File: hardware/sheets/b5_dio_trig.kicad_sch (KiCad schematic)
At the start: 26 parts, among them J7 Panel link 2x20 female, J8 Panel link 2x20 female, U501 SN74AHCT541PWR, U502 74HCT125PW, U503 SN74LVC1T45DBVR, U505 TCA9535PWR

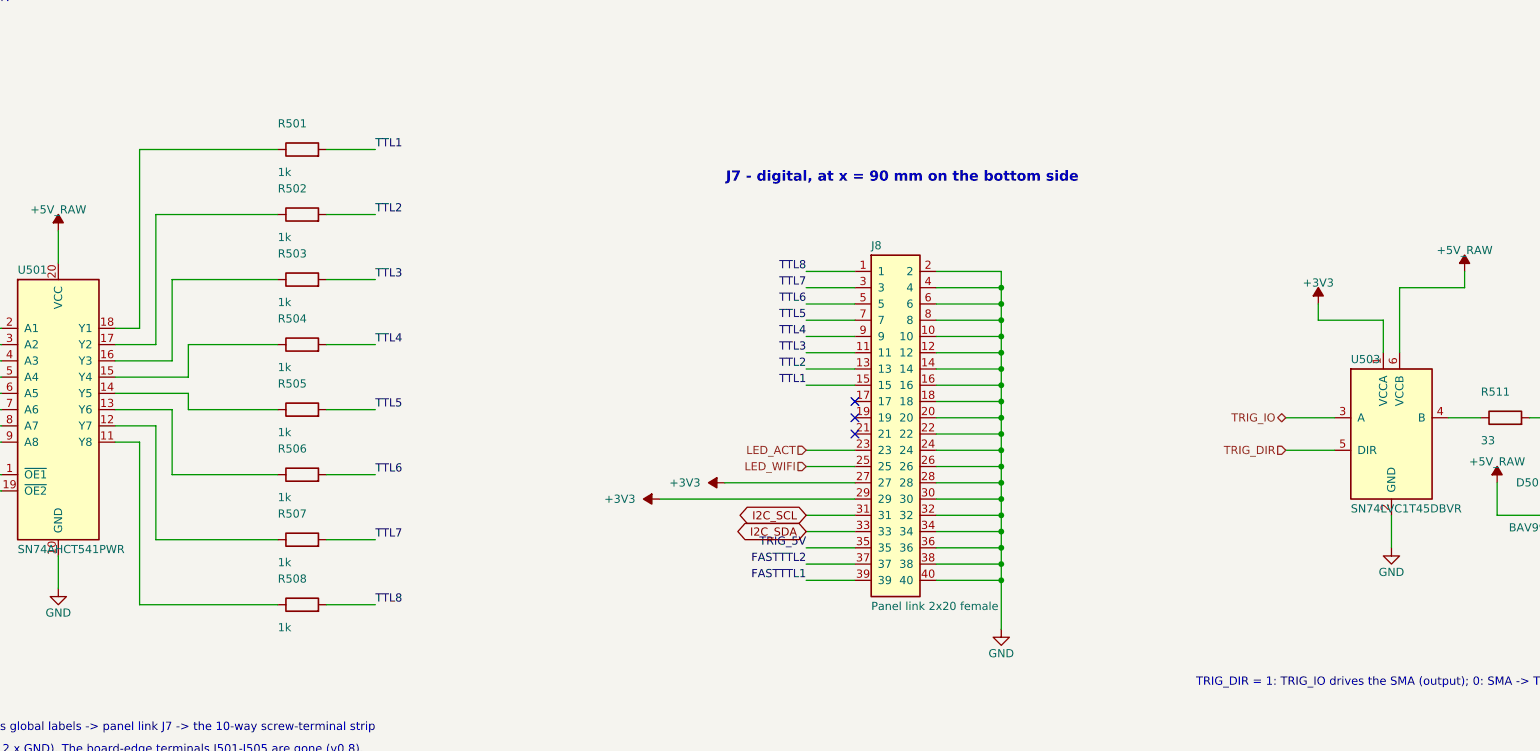
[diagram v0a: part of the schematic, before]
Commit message: b5: TTL series resistors R501-R508 as two 4 x 1k arrays RN501/RN502 (0603x4, C20197); U501 outputs labelled TTL1_Y..TTL8_Y (user request); same connectivity, ERC unchanged
Co-Authored-By: Claude Fable 5.1 <noreply@anthropic.com>
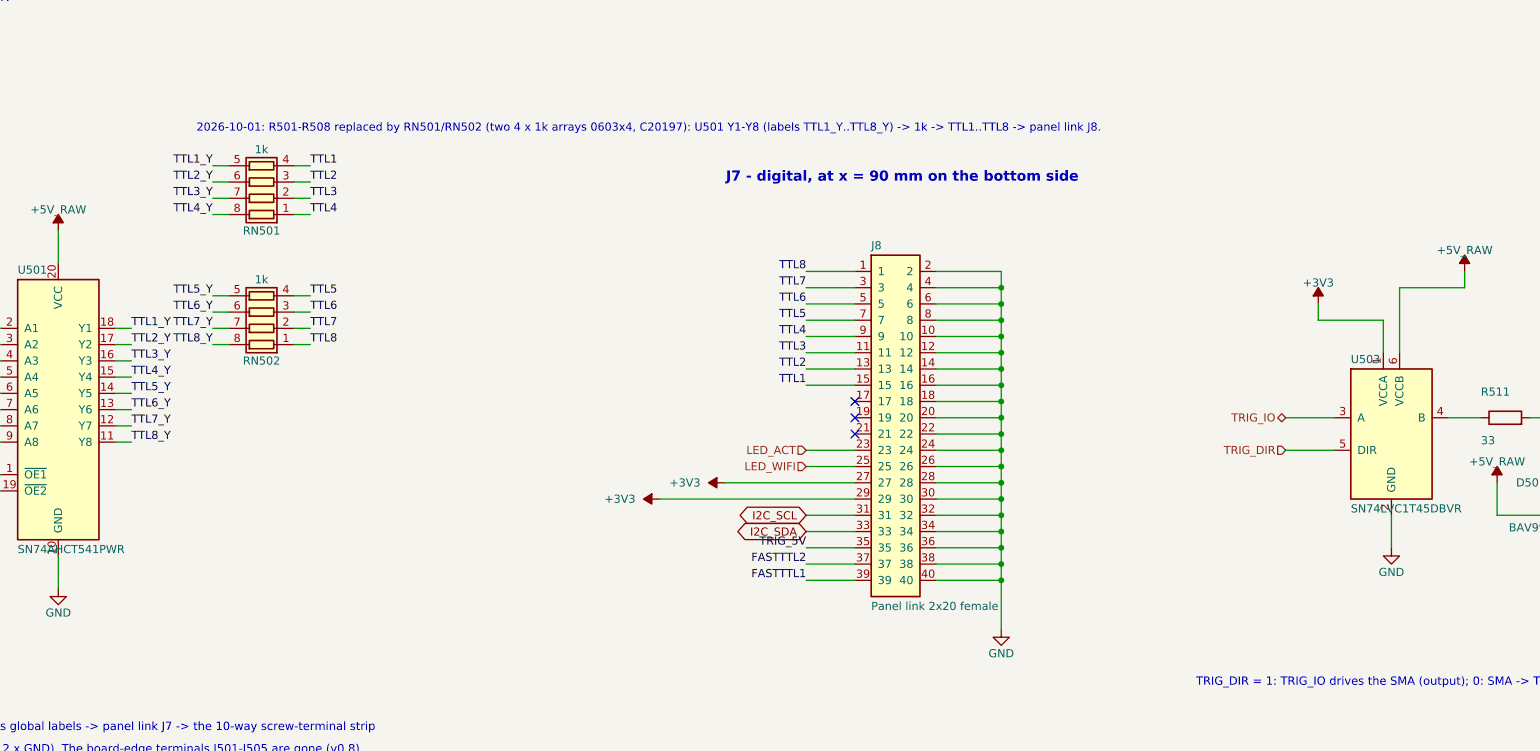
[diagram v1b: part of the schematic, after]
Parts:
- removed R501, R502, R503, R504, R505, R506, R507, R508: 1k, Resistor_SMD:R_0603_1608Metric, symbol class_board:R0603_1k
- added RN501, RN502: 1k, Resistor_SMD:R_Array_Convex_4x0603, symbol Device:R_Pack04
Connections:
- net TTL1: now also RN501.4 (R4.1)
- net TTL2: now also RN501.3 (R3.1)
- net TTL3: now also RN501.2 (R2.1)
- net TTL4: now also RN501.1 (R1.1)
- net TTL5: now also RN502.4 (R4.1)
- net TTL6: now also RN502.3 (R3.1)
- net TTL7: now also RN502.2 (R2.1)
- net TTL8: now also RN502.1 (R1.1)
- net TTL7_Y: now reaches U501.12 (Y7)
- net TTL7_Y: now also RN502.7 (R2.2)
- net TTL8_Y: now reaches U501.11 (Y8)
- net TTL8_Y: now also RN502.8 (R1.2)
- net TTL6_Y: now reaches U501.13 (Y6)
- net TTL6_Y: now also RN502.6 (R3.2)
- net TTL5_Y: now reaches U501.14 (Y5)
- net TTL5_Y: now also RN502.5 (R4.2)
- net TTL4_Y: now reaches U501.15 (Y4)
- net TTL4_Y: now also RN501.8 (R1.2)
- net TTL3_Y: now reaches U501.16 (Y3)
- net TTL3_Y: now also RN501.7 (R2.2)
- net TTL2_Y: now reaches U501.17 (Y2)
- net TTL2_Y: now also RN501.6 (R3.2)
- net TTL1_Y: now reaches U501.18 (Y1)
- net TTL1_Y: now also RN501.5 (R4.2)
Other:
- note added: "2026-10-01: R501-R508 replaced by RN501/RN502 (two 4 x 1k arrays 0603x4, C20197): U501 Y1-Y8 (labels TTL1_Y..TTL8_Y) -> 1k -> TTL1..TTL8 -> panel link J8."

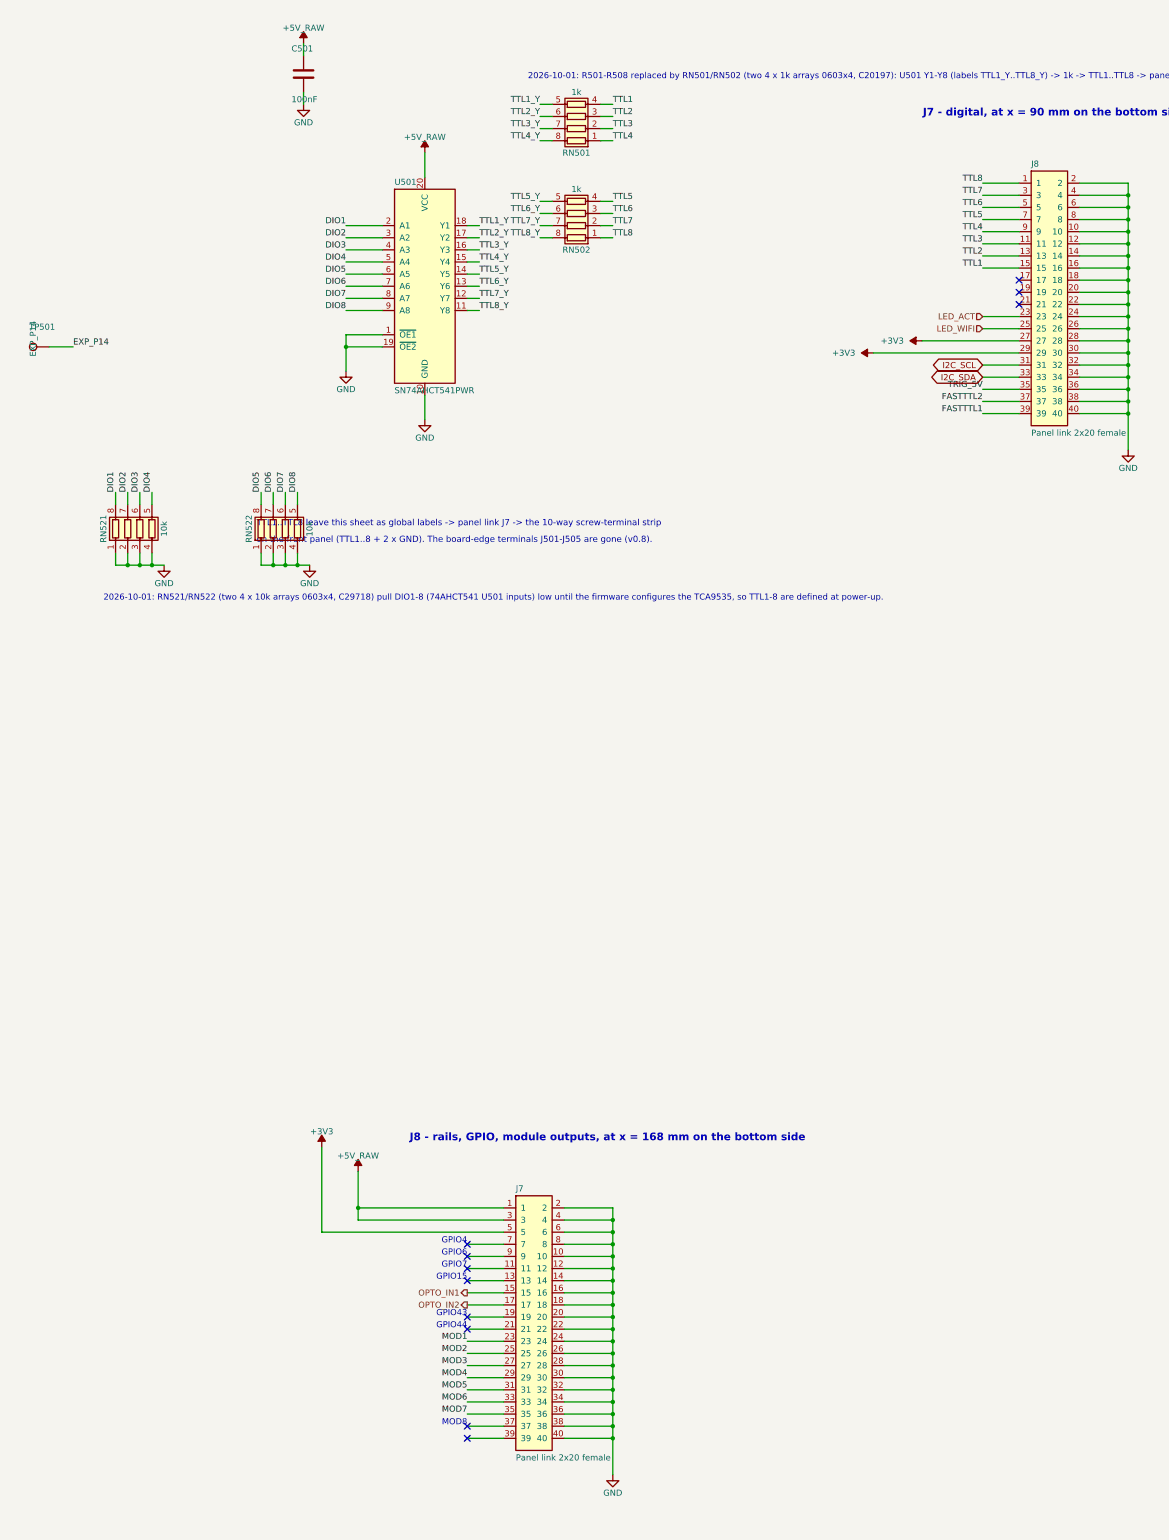
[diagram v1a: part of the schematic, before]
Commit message: hardware: instructor 2026-10-01 saves synced (one GND net on both boards, PCB updated, R951-R958, headers DNP per Decision #73) + nmr_tx R808 -> TX_VMID, C813 removed, R805/R806 10 k (review B2)
Co-Authored-By: Claude Fable 5.1 <noreply@anthropic.com>
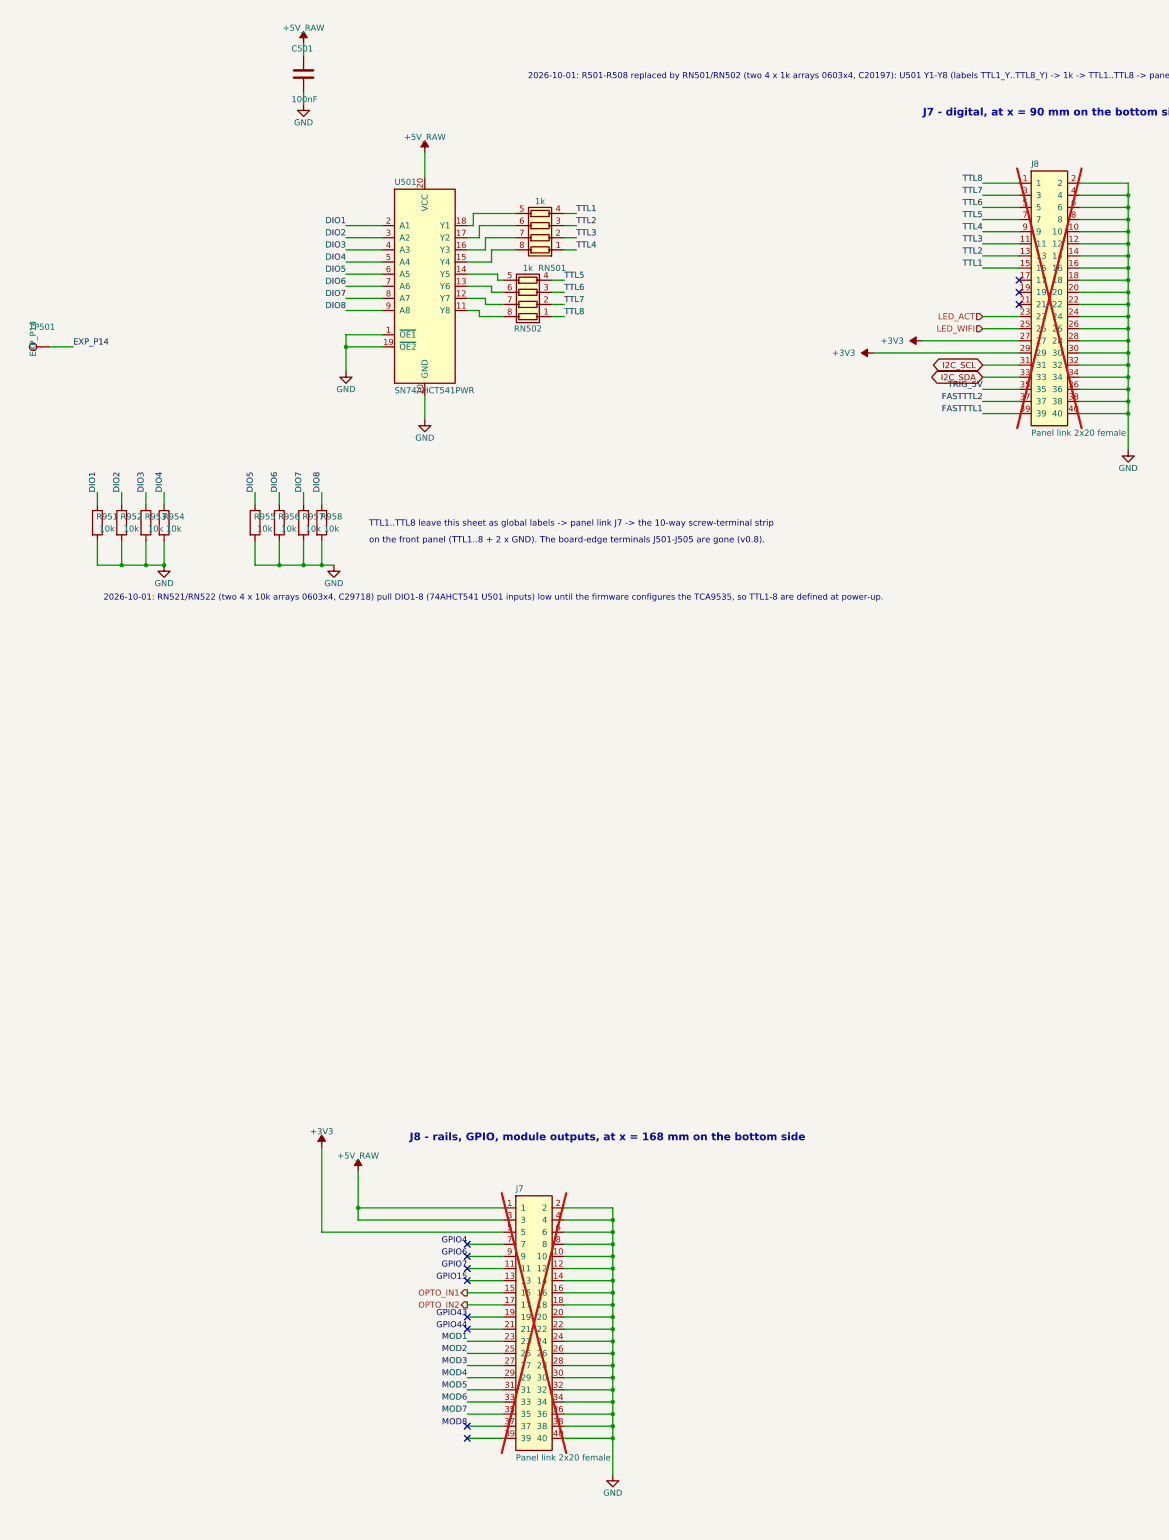
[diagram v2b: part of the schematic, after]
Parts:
- removed RN521, RN522: 10k, Resistor_SMD:R_Array_Convex_4x0603, symbol Device:R_Pack04
- added R951, R952, R953, R954, R955, R956, R957, R958: 10k, Resistor_SMD:R_0603_1608Metric, symbol class_board:R0603_10k
- J7, J8: now not fitted
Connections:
- net DIO1: now also R951.1
- net DIO2: now also R952.1
- net DIO3: now also R953.1
- net DIO4: now also R954.1
- net DIO5: now also R955.1
- net DIO6: now also R956.1
- net DIO7: now also R957.1
- net DIO8: now also R958.1
- net GND: now also R951.2, R952.2, R953.2, R954.2, R955.2, R956.2, R957.2, R958.2
- net TTL1_Y: no longer names the net of RN501.5 (R4.2), U501.18 (Y1)
- net TTL2_Y: no longer names the net of RN501.6 (R3.2), U501.17 (Y2)
- net TTL3_Y: no longer names the net of RN501.7 (R2.2), U501.16 (Y3)
- net TTL4_Y: no longer names the net of RN501.8 (R1.2), U501.15 (Y4)
- net TTL5_Y: no longer names the net of RN502.5 (R4.2), U501.14 (Y5)
- net TTL6_Y: no longer names the net of RN502.6 (R3.2), U501.13 (Y6)
- net TTL7_Y: no longer names the net of RN502.7 (R2.2), U501.12 (Y7)
- net TTL8_Y: no longer names the net of RN502.8 (R1.2), U501.11 (Y8)
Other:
- moved on the sheet: RN501, RN502

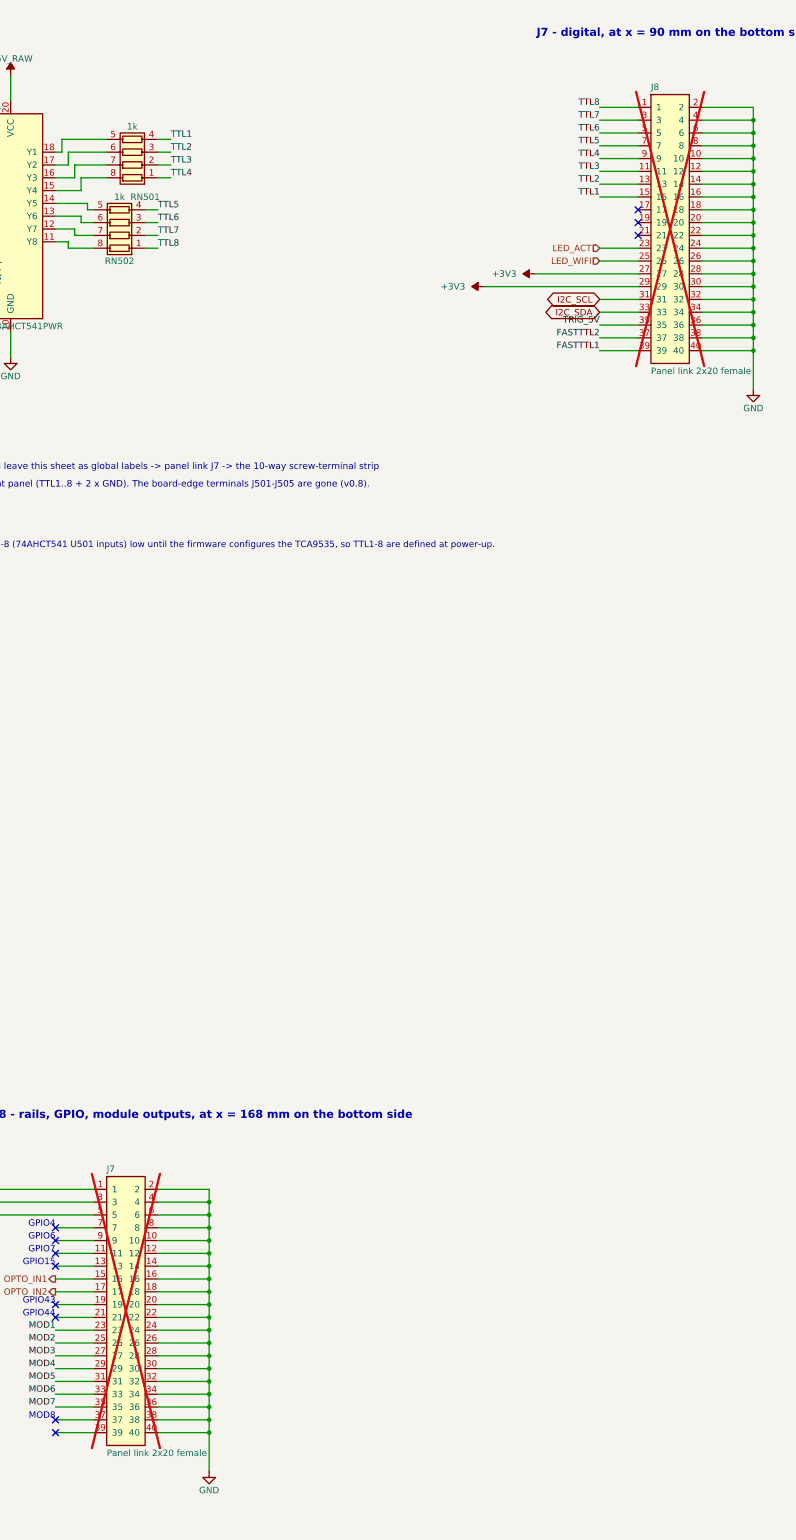
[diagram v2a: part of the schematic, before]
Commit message: Final boards (2026-10-01 23:44/23:48 saves) and re-exported release STEP models
- class-board and front-panel: DNP + out-of-BOM flags on the hand-soldered connectors, panel 3D-model paths on TIGP_BOARD_LIB, schematic sheets in step
- hardware/release: class-board.step and front-panel.step re-exported from these boards (filters as before, now without --no-dnp so the hand-soldered connectors keep their bodies; panel exported directly, no path-redirect copy); the STL meshes are unchanged (same triangles and bounding boxes)
- README: export note

Co-Authored-By: Claude Fable 5.1 <noreply@anthropic.com>
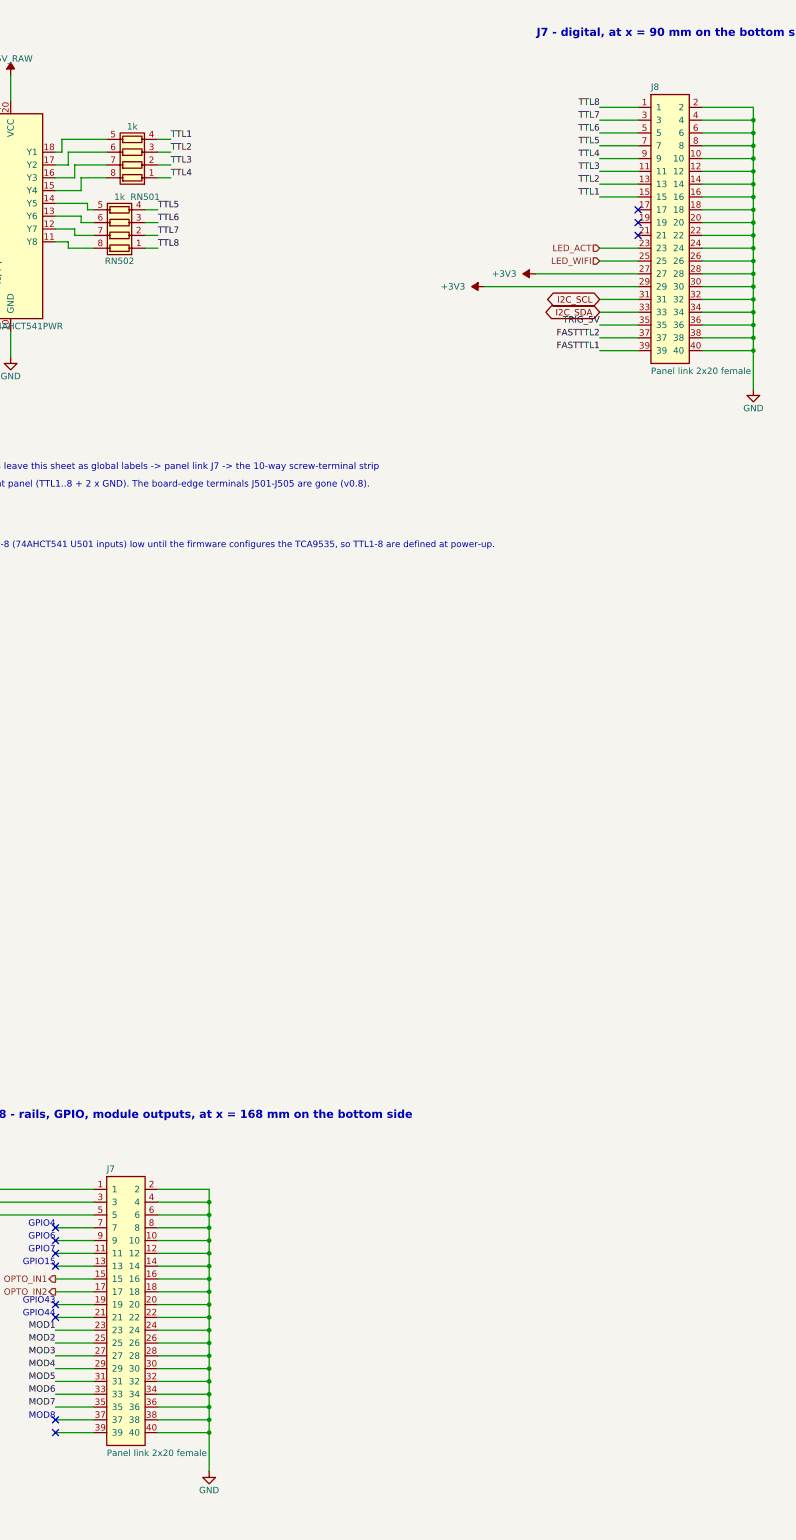
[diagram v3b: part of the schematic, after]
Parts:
- J7, J8: now fitted; now in the parts list
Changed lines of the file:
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@@
 		(body_style 1)
 		(exclude_from_sim no)
-		(in_bom no)
+		(in_bom yes)
 		(on_board yes)
 		(in_pos_files yes)
-		(dnp yes)
+		(dnp no)
 		(fields_autoplaced yes)
 		(property "Reference" "J7"
@@
 		(body_style 1)
 		(exclude_from_sim no)
-		(in_bom no)
+		(in_bom yes)
 		(on_board yes)
 		(in_pos_files yes)
-		(dnp yes)
+		(dnp no)
 		(property "Reference" "J8"
 			(at 349.25 76.708 0)
